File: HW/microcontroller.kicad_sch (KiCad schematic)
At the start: 2 parts, among them J1 AVR-ISP-6, U1 ATmega88P-20A

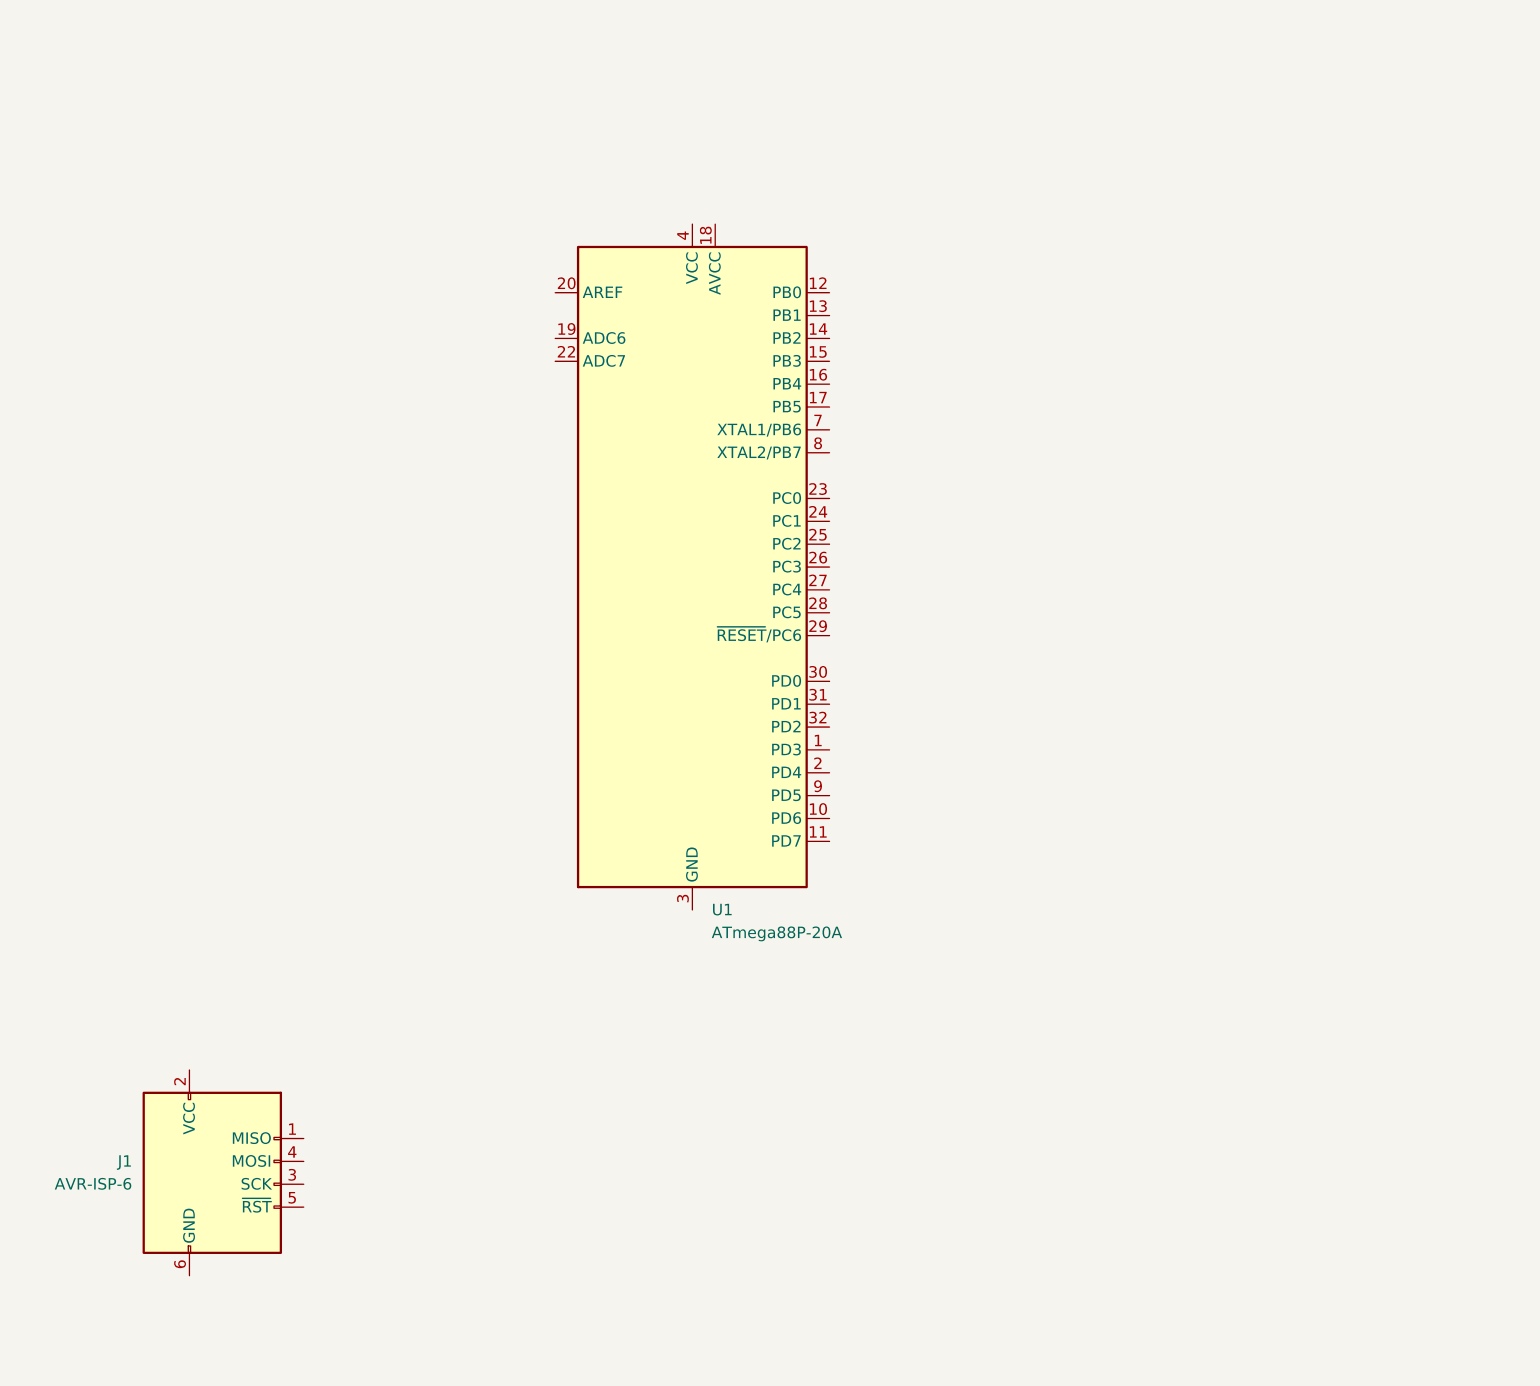
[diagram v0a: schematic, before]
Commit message: update schematic
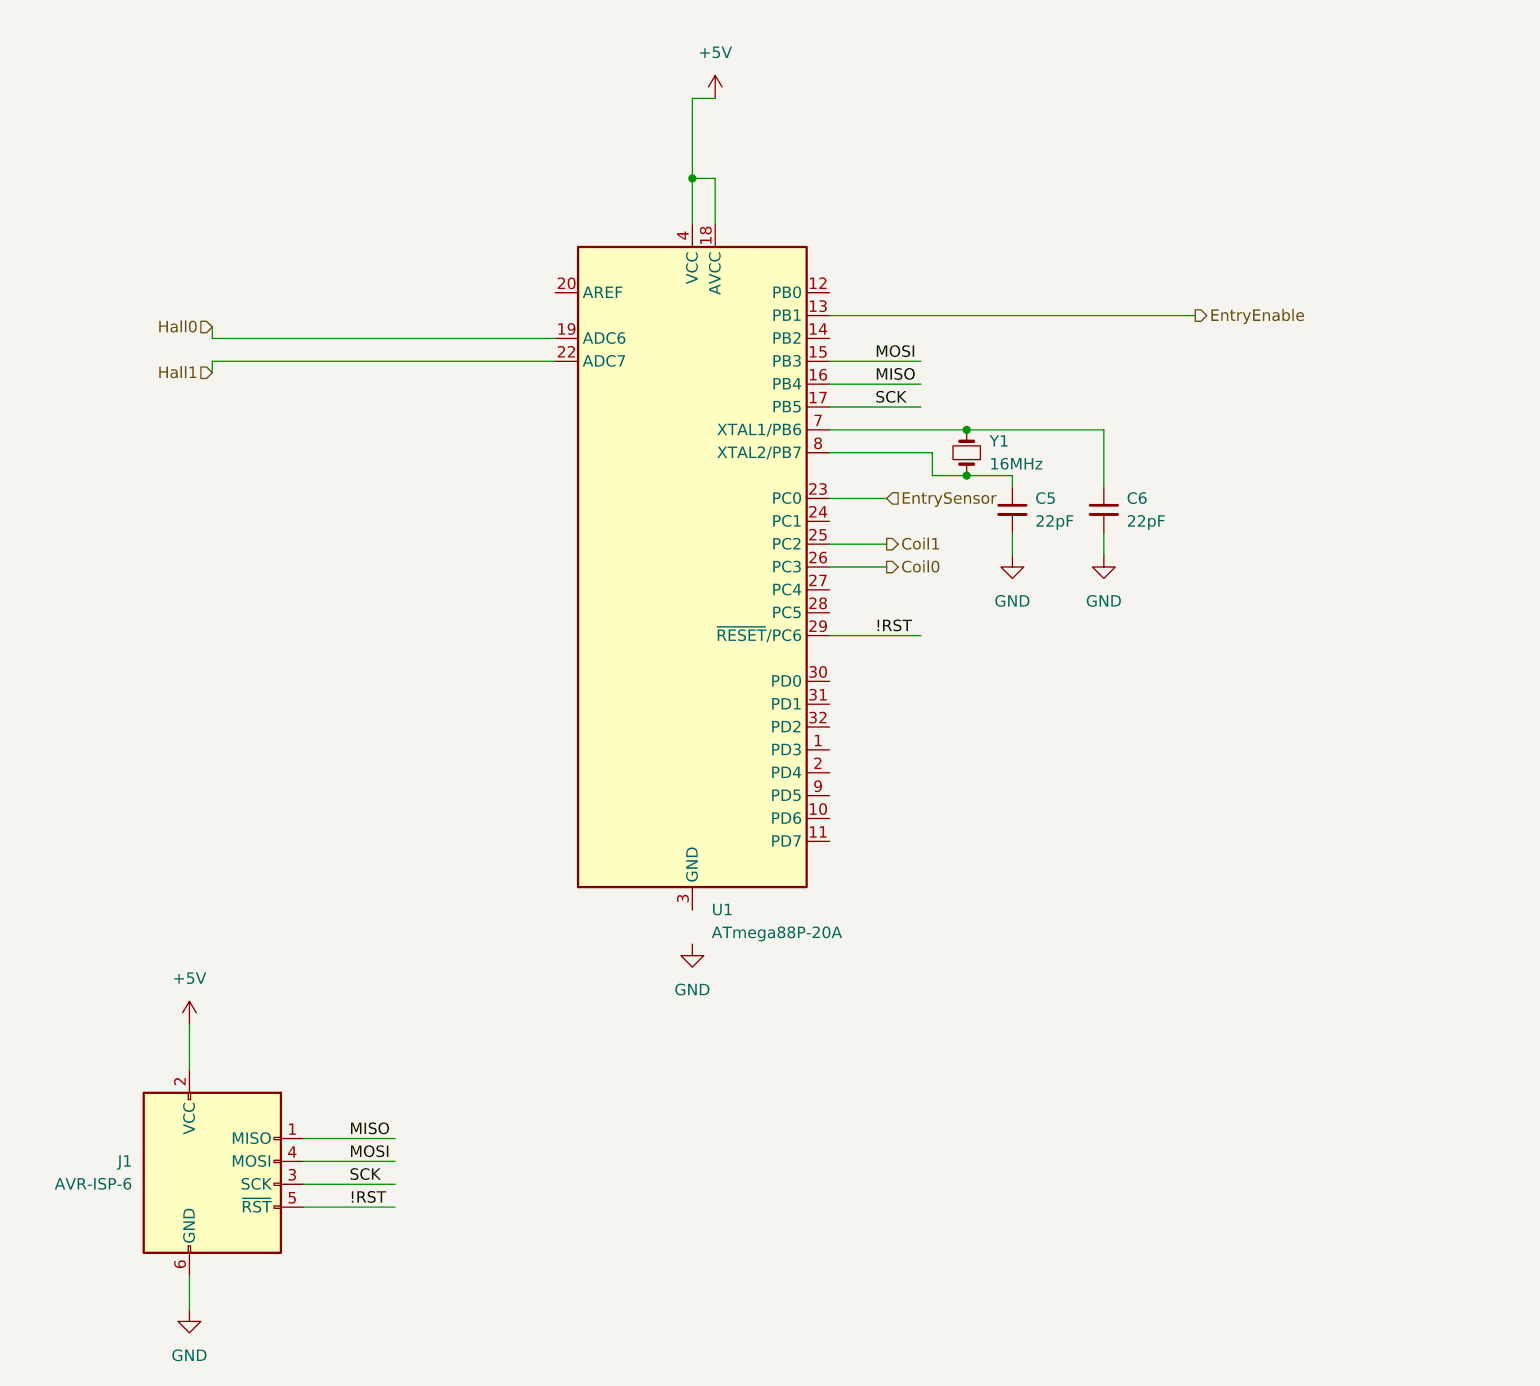
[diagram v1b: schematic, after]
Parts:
- added C5, C6: 22pF, Capacitor_SMD:C_0603_1608Metric_Pad1.08x0.95mm_HandSolder, symbol Device:C_Small
- added Y1: 16MHz, Crystal:Crystal_HC49-U_Vertical, symbol Device:Crystal_Small
- J1: footprint (none) -> Connector_PinHeader_2.54mm:PinHeader_2x03_P2.54mm_Vertical
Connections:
- net MISO: now reaches J1.1 (MISO)
- net MISO: now also U1.16 (PB4)
- net +5V: now reaches J1.2 (VCC)
- net +5V: now also U1.18 (AVCC), U1.4 (VCC), U1.6 (VCC)
- net SCK: now reaches J1.3 (SCK)
- net SCK: now also U1.17 (PB5)
- net MOSI: now reaches J1.4 (MOSI)
- net MOSI: now also U1.15 (PB3)
- net !RST: now reaches J1.5 (~{RST})
- net !RST: now also U1.29 (~{RESET}/PC6)
- net GND: now reaches J1.6 (GND)
- net GND: now also C5.2, C6.2
- net EntryEnable: now reaches U1.13 (PB1)
- net Hall0: now reaches U1.19 (ADC6)
- net Hall1: now reaches U1.22 (ADC7)
- net EntrySensor: now reaches U1.23 (PC0)
- net Coil1: now reaches U1.25 (PC2)
- net Coil0: now reaches U1.26 (PC3)
- net at U1.7 (XTAL1/PB6): now also C6.1, Y1.2
- net at U1.8 (XTAL2/PB7): now also C5.1, Y1.1

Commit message: update HW, reduce board to 5x5 cm
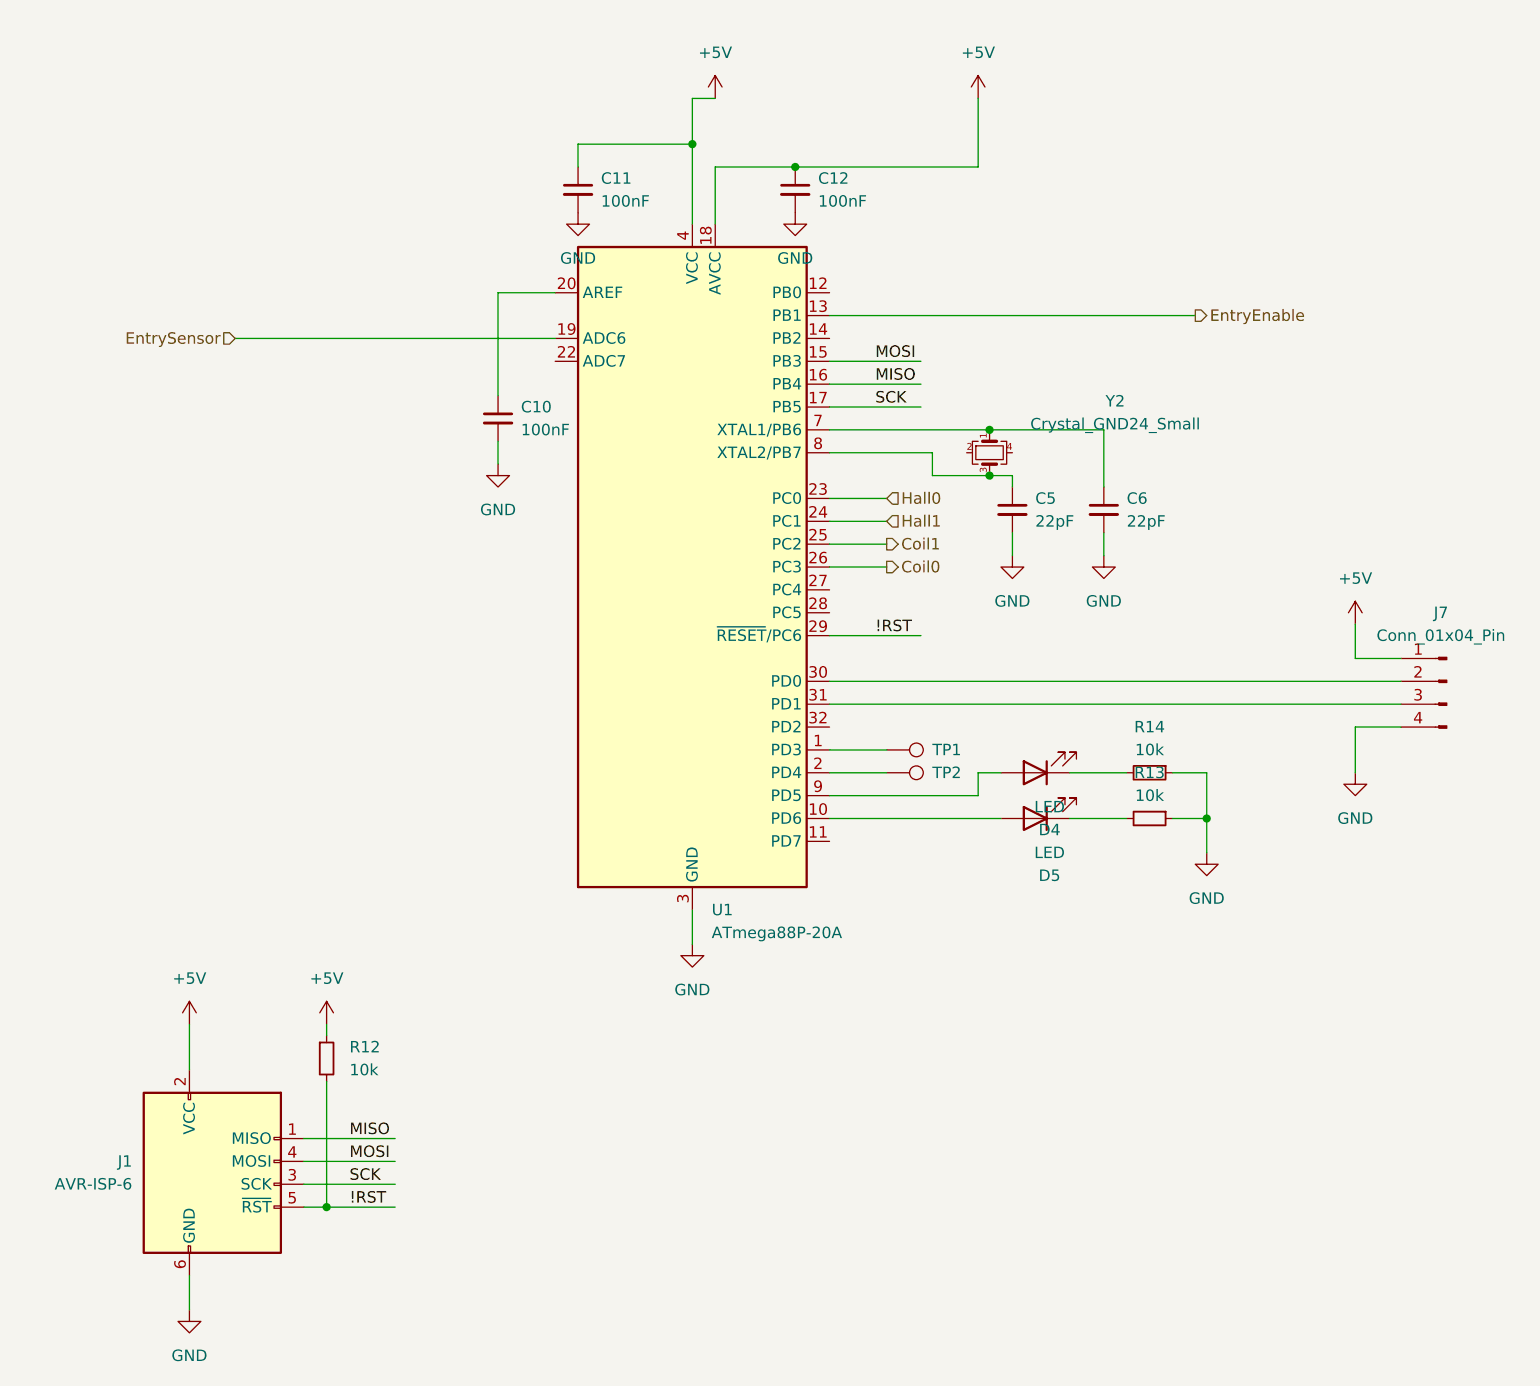
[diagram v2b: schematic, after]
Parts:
- removed Y1: 16MHz, Crystal:Crystal_HC49-U_Vertical, symbol Device:Crystal_Small
- added C10, C11, C12: 100nF, Capacitor_SMD:C_0603_1608Metric_Pad1.08x0.95mm_HandSolder, symbol Device:C_Small
- added D4, D5: LED, LED_SMD:LED_PLCC-2_3.4x3.0mm_KA, symbol Device:LED
- added J7: Conn_01x04_Pin, Connector_JST:JST_XH_B4B-XH-A_1x04_P2.50mm_Vertical, symbol Connector:Conn_01x04_Pin
- added R12, R13, R14: 10k, Resistor_SMD:R_0603_1608Metric_Pad0.98x0.95mm_HandSolder, symbol Device:R_Small
- added TP1, TP2: TestPoint, TestPoint:TestPoint_Pad_D2.0mm, symbol Connector:TestPoint
- added Y2: Crystal_GND24_Small, Crystal:Crystal_SMD_3225-4Pin_3.2x2.5mm_HandSoldering, symbol Device:Crystal_GND24_Small
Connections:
- net !RST: now also R12.2
- net +5V: now also C11.1, C12.1, J7.1 (Pin_1), R12.1
- net EntrySensor: now also U1.19 (ADC6); no longer U1.23 (PC0)
- net GND: now also U1.21 (GND), U1.3 (GND), U1.5 (GND), C10.2, C11.2, C12.2, J7.4 (Pin_4), R13.1, R14.1
- net Hall0: now also U1.23 (PC0); no longer U1.19 (ADC6)
- net Hall1: now also U1.24 (PC1); no longer U1.22 (ADC7)
- net at C6.1, U1.7 (XTAL1/PB6): now also Y2.1
- net at C5.1, U1.8 (XTAL2/PB7): now also Y2.3
- net at U1.1 (PD3): now also TP1.1
- net at U1.10 (PD6): now also D5.2 (A)
- net at U1.2 (PD4): now also TP2.1
- net at U1.20 (AREF): now also C10.1
- net at U1.30 (PD0): now also J7.2 (Pin_2)
- net at U1.31 (PD1): now also J7.3 (Pin_3)
- net at U1.9 (PD5): now also D4.2 (A)
- new net: D5.1 (K), R13.2
- new net: D4.1 (K), R14.2

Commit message: update HW
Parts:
- added L1: 10µH, Inductor_SMD:L_0603_1608Metric_Pad1.05x0.95mm_HandSolder, symbol Device:L_Small
- added R16: 30k, Resistor_SMD:R_0603_1608Metric_Pad0.98x0.95mm_HandSolder, symbol Device:R_Small
- added R17: 10k, Resistor_SMD:R_0603_1608Metric_Pad0.98x0.95mm_HandSolder, symbol Device:R_Small
- added TP3: TestPoint, TestPoint:TestPoint_Pad_D2.0mm, symbol Connector:TestPoint
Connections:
- net +5V: now also L1.2; no longer C12.1, U1.18 (AVCC)
- net GND: now also R17.2
- net at U1.22 (ADC7): now also R16.2, R17.1
- net at U1.27 (PC4): now also TP3.1
- new net: C12.1, L1.1, U1.18 (AVCC)
- new net Vdrive: R16.1

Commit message: update schematic and board
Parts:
- renumbered C11 to C1, C12 to C2, C10 to C3, C5 to C4, C6 to C5, D4 to D1, D5 to D2, J7 to J6, J1 to J7, R12 to R10, R16 to R6, R17 to R7, R14 to R8, R13 to R9, TP3 to TP1, TP1 to TP2, TP2 to TP3, U1 to U2, Y2 to Y1

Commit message: finished first layout
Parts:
- added C6: 100nF, Capacitor_SMD:C_0603_1608Metric_Pad1.08x0.95mm_HandSolder, symbol Device:C_Small
- renumbered R9 to R8, R8 to R9
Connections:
- net EntryEnable: now also U2.9 (PD5); no longer U2.13 (PB1)
- net EntrySensor: now also U2.24 (PC1); no longer U2.19 (ADC6)
- net GND: now also C6.2
- net Hall0: now also U2.22 (ADC7); no longer U2.23 (PC0)
- net Hall1: now also U2.23 (PC0); no longer U2.24 (PC1)
- net at R6.2, R7.1: now also U2.19 (ADC6), C6.1; no longer U2.22 (ADC7)
- net at D2.2 (A): now also U2.11 (PD7); no longer U2.10 (PD6)
- net at D1.2 (A): now also U2.10 (PD6); no longer U2.9 (PD5)
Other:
- moved on the sheet: D1, D2, R6, R7, R8, R9

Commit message: first HW order state
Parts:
- J6: value Conn_01x04_Pin -> UART; footprint Connector_JST:JST_XH_B4B-XH-A_1x04_P2.50mm_Vertical -> Connector_PinHeader_2.54mm:PinHeader_1x04_P2.54mm_Vertical
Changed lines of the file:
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@@
 			)
 		)
-		(property "Value" "Conn_01x04_Pin"
+		(property "Value" "UART"
 			(at 200.025 91.44 0)
 			(effects
@@
 			)
 		)
-		(property "Footprint" "Connector_JST:JST_XH_B4B-XH-A_1x04_P2.50mm_Vertical"
+		(property "Footprint" "Connector_PinHeader_2.54mm:PinHeader_1x04_P2.54mm_Vertical"
 			(at 200.66 96.52 0)
 			(effects
